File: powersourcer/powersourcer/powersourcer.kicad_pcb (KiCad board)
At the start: 2 copper layers, 47 parts, among them Q1 2N2222, Q10 TIP35C, Q2 TIP122, Q3 TIP35C, Q4 TIP35C, Q5 TIP35C, Q6 TIP35C, Q7 TIP35C, Q8 TIP35C, Q9 TIP35C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

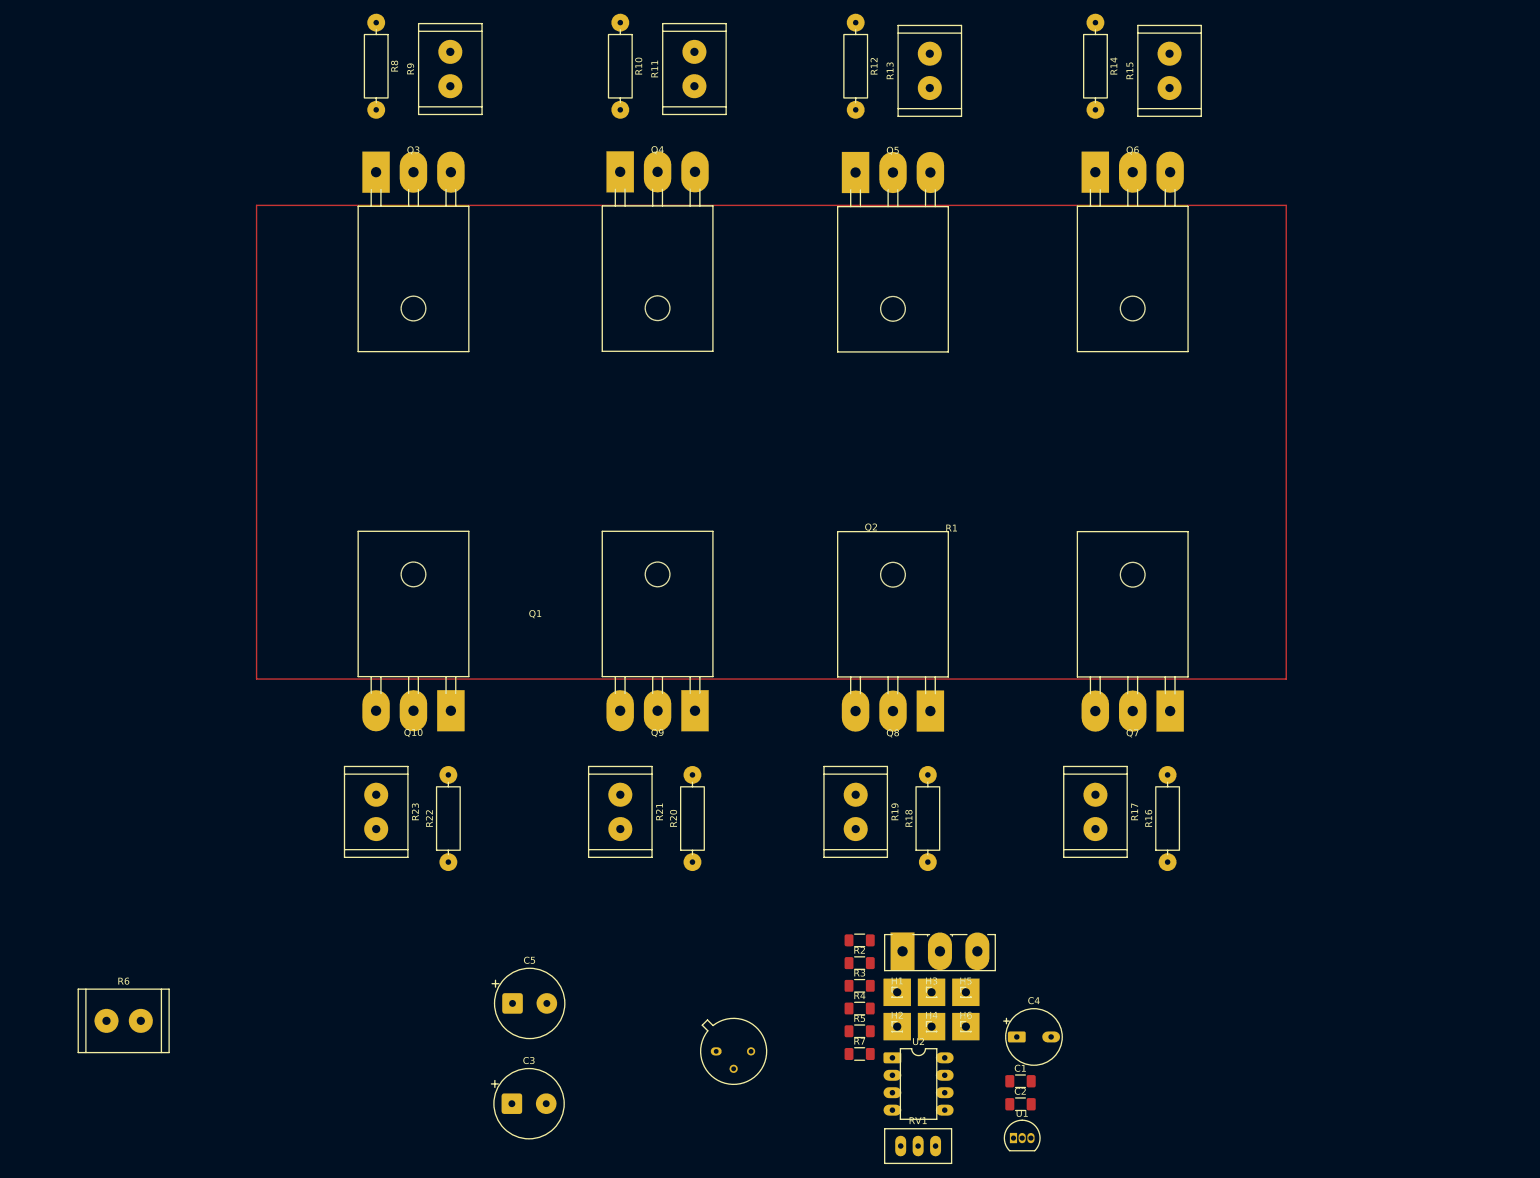
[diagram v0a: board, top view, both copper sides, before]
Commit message: Práce na pcb. Odstraněny plošky pro externí resistor.
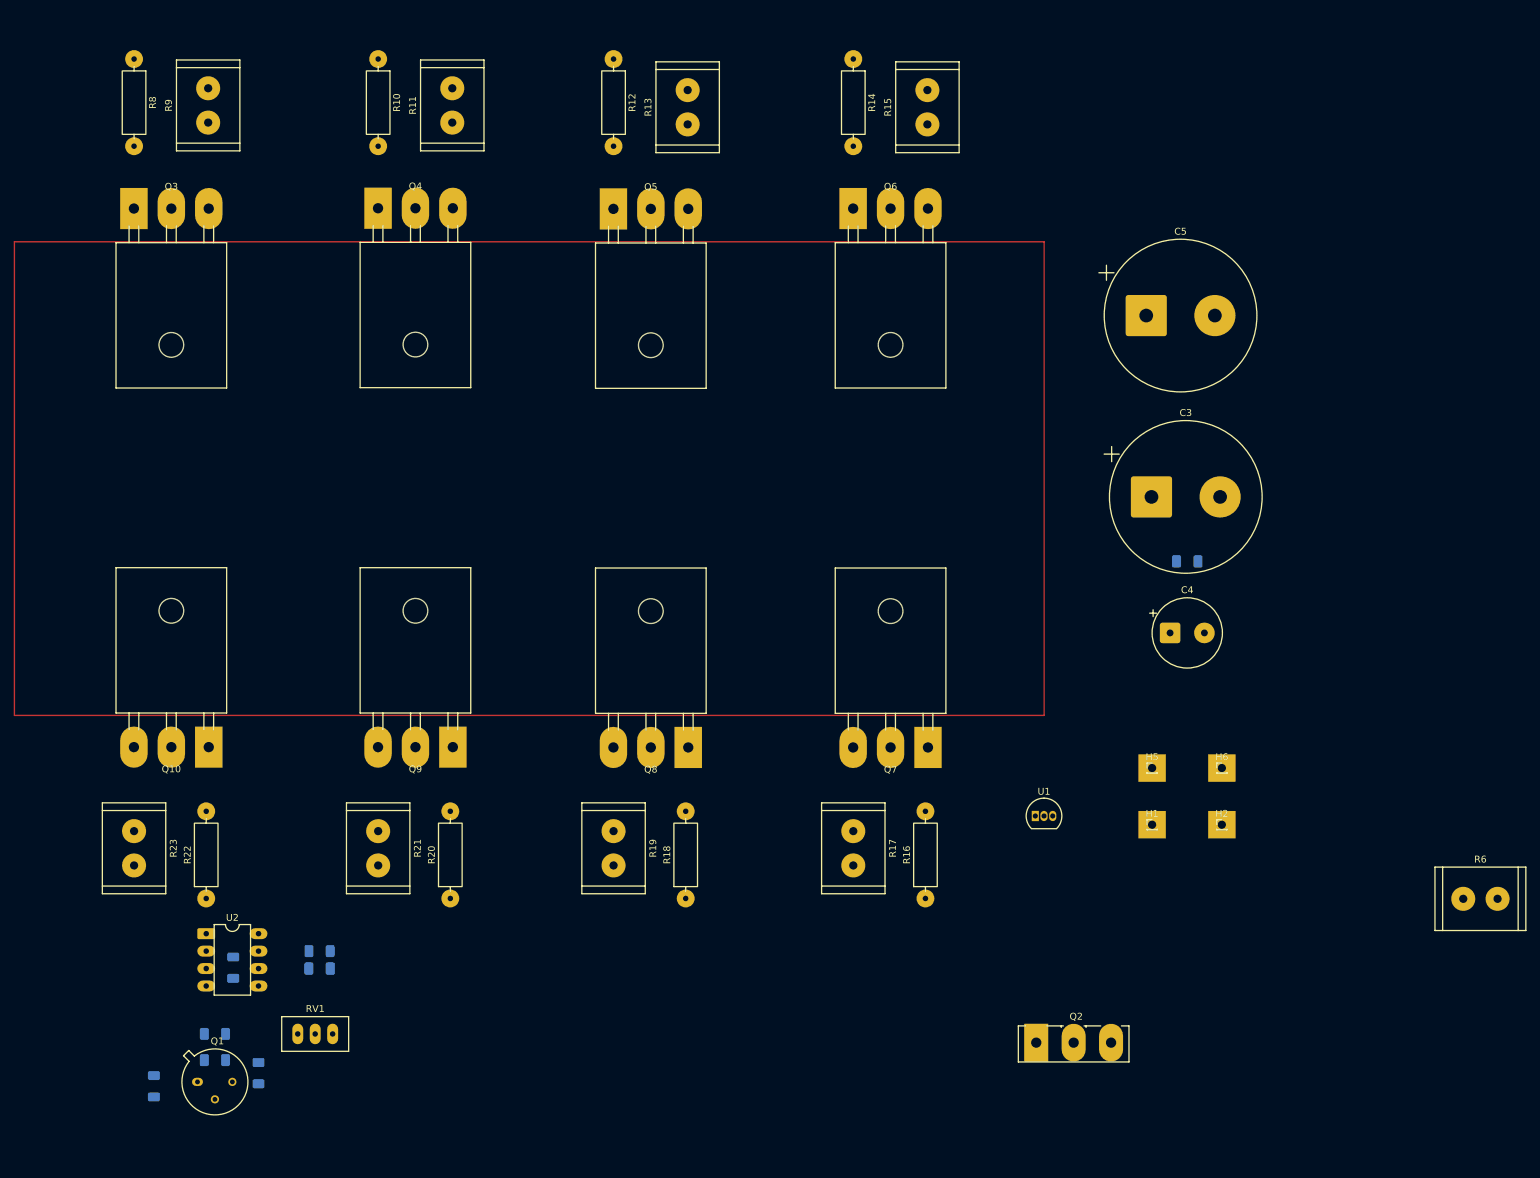
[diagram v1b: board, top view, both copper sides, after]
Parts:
- removed H3: 25W_1, HAM_Lib:PinHeader_1x01_P1.00mm_Vertical
- removed H4: 25W_2, HAM_Lib:PinHeader_1x01_P1.00mm_Vertical
- C1, C2, R1, R2, R3, R4, R5, R7: moved to B.Cu
- C3, C5: footprint HAM_Lib:CP_Radial_D10.0mm_P5.00mm -> HAM_Lib:CP_Radial_D22.0mm_P10.00mm_SnapIn
- C4: footprint HAM_Lib:CP_Radial_D8.0mm_P5.00mm -> HAM_Lib:CP_Radial_D10.0mm_P5.00mm
- moved R6 198.4 mm to (226.9, 154.3)
- moved C5 136.2 mm to (180.8, 69.3)
- moved C3 128.4 mm to (181.5, 95.8)
- moved C1 103.4 mm to (60.3, 164.5), turned to 180 degrees
- moved R7 102.9 mm to (36.2, 181.6), turned to 90 degrees
- moved U2 101.6 mm to (43.8, 159.4)
- moved R4 94.2 mm to (45.1, 177.8)
- moved R3 94.2 mm to (45.1, 174.0)
- moved R1 91.3 mm to (47.8, 164.3), turned to 90 degrees
- moved RV1 89.3 mm to (62.2, 174.0)
- moved R5 87.8 mm to (51.4, 179.7), turned to -90 degrees
- moved C2 82.7 mm to (186.7, 105.2)
- moved R2 78.7 mm to (60.3, 161.9), turned to 180 degrees
- moved Q1 75.7 mm to (42.5, 181.0)
- moved C4 63.0 mm to (184.2, 115.6)
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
